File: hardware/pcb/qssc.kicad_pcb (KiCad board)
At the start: 4 copper layers, 130 x 85 mm, 75 parts, among them J1 FT232RL, J10 USB-C, J2 5V Barrel, J3 SMA, J4 Emitter drv, J5 Detector FE, J6 DET_BIAS, J7 RESET, J8 MW_GATE, J9 JTAG, U1 XC7A35T-1CPG236C, U3 ADF4351BCPZ, U5 HMC441LP3E, U7 ADA4530-1, Y1 100MHz TCXO

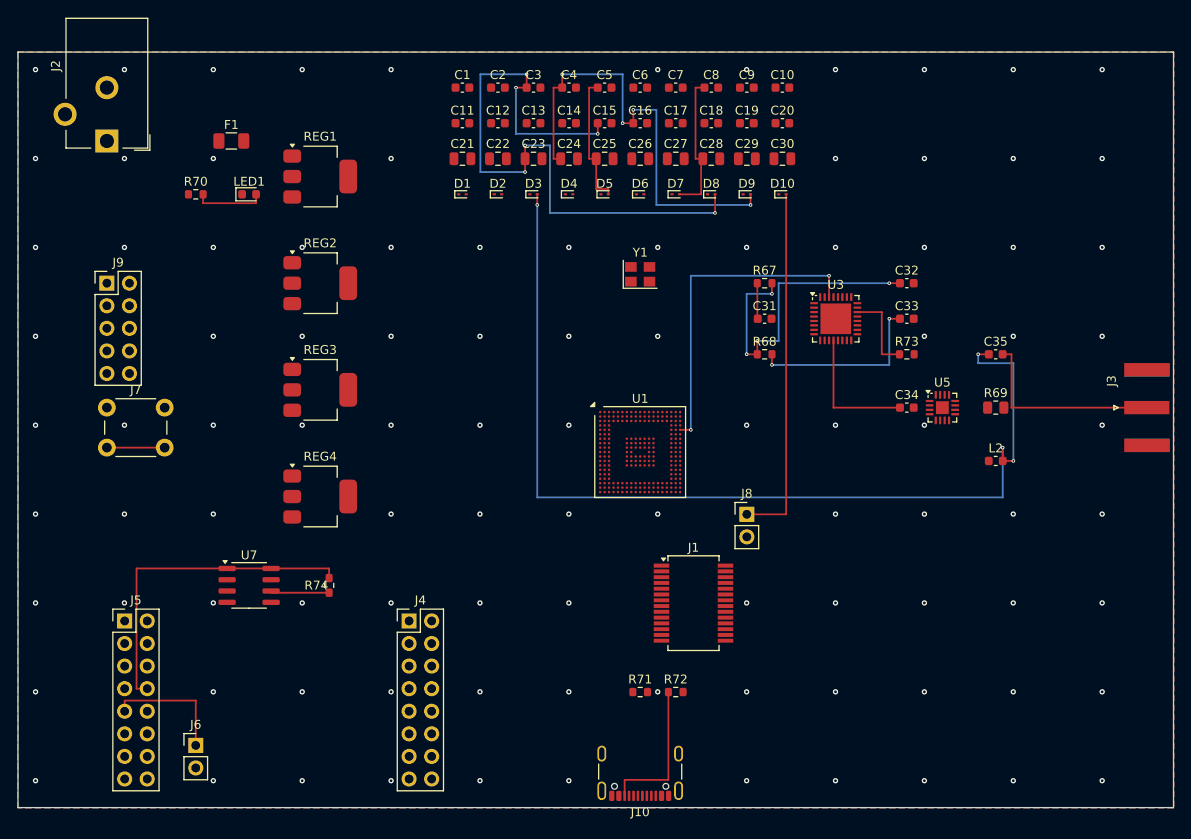
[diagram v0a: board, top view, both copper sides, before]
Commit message: pcb: fix FPGA GND-ball netting (52 balls were wrongly +3V3) + full CPG236 ball map
The FPGA power/ground net map was missing the "GND" key in _FPGA_PWR_NET,
so all 52 GND balls fell through the `else "+3V3"` branch (intended only for
VCCO_* banks) and were netted +3V3 — electrically wrong though DRC appeared
clean (all pads on the same wrong net, no conflict).

Fix: add "GND":"GD" to _FPGA_PWR_NET. Now A1/W1/... -> GND as datasheet
intended.

Verified:
  fpga_net_map(): A1->GND, W1->GND, GND=67 balls, +3V3=30, +1V0=8, +1V8=3
  saved PCB sexp: 157 pads netted (67 GND/30 +3V3/8 +1V0/3 +1V8), 81 NC spare-IO
  kicad-cli pcb drc: 0 violations, 0 unconnected, 0 footprint errors

Co-Authored-By: Claude <noreply@anthropic.com>
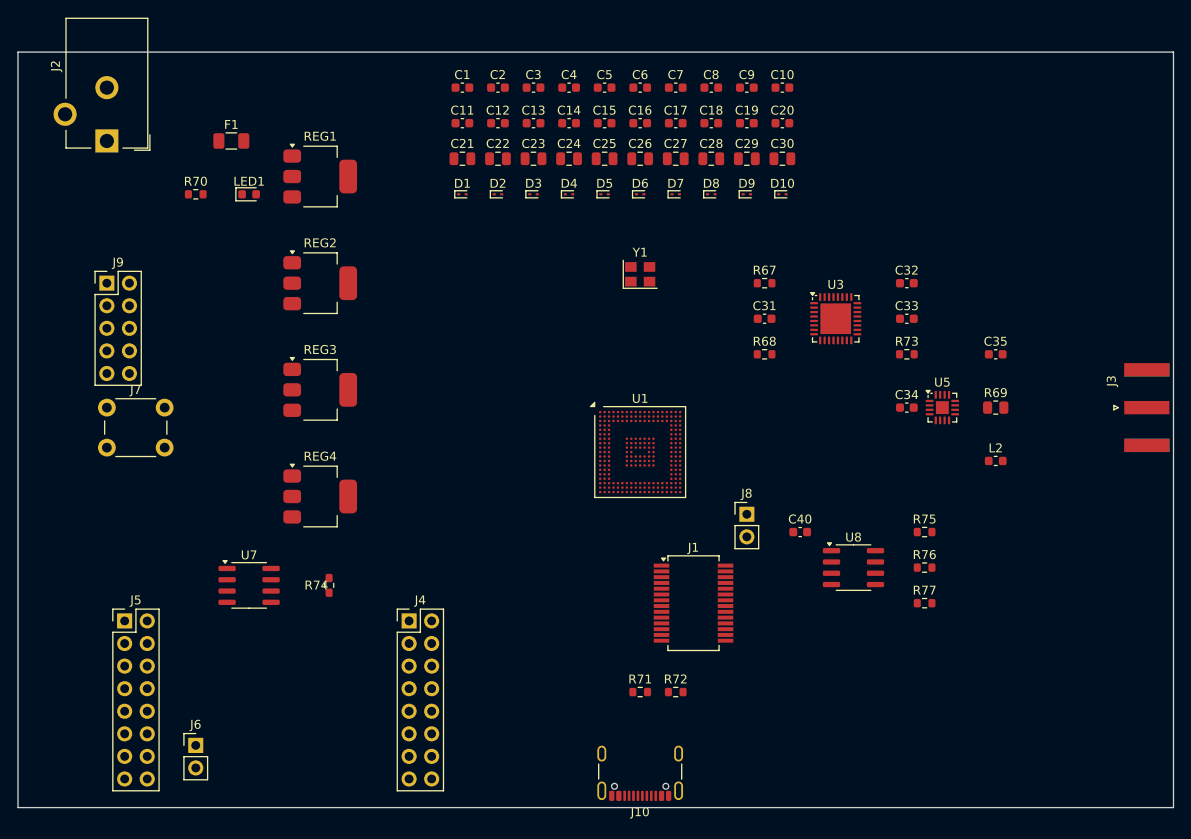
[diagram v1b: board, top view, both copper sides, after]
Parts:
- added C40: 100nF, C_0603_1608Metric, F.Cu at (88.0, 54.0)
- added R75: 4.7k, R_0603_1608Metric, F.Cu at (102.0, 54.0)
- added R76: 4.7k, R_0603_1608Metric, F.Cu at (102.0, 58.0)
- added R77: 4.7k, R_0603_1608Metric, F.Cu at (102.0, 62.0)
- added U8: W25Q128JVSIQ, SOIC-8_3.9x4.9mm_P1.27mm, F.Cu at (94.0, 58.0)
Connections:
- U1 pad A1: (no net) -> GND
- U1 pad A12: (no net) -> TIA_OUT
- U1 pad A13: (no net) -> GND
- U1 pad A14: (no net) -> refclk_out
- U1 pad A15: (no net) -> mod_sync
- U1 pad A16: (no net) -> clk_100mhz
- U1 pad A17: (no net) -> mw_gate
- U1 pad A18: (no net) -> SPI_CLK
- U1 pad A19: (no net) -> GND
- U1 pad A3: (no net) -> GND
- U1 pad A5: (no net) -> GND
- U1 pad A7: (no net) -> GND
- U1 pad A9: (no net) -> GND
- U1 pad B1: (no net) -> GND
- U1 pad B12: (no net) -> VREFP
- U1 pad B13: (no net) -> GND
- U1 pad B14: (no net) -> GND
- U1 pad B15: (no net) -> SPI_DATA
- U1 pad B16: (no net) -> ADF_MUXOUT
- U1 pad B17: (no net) -> emitter_rows0
- U1 pad B18: (no net) -> emitter_rows3
- U1 pad B19: (no net) -> +3V3
- U1 pad B3: (no net) -> GND
- U1 pad B5: (no net) -> GND
- U1 pad B7: (no net) -> GND
- U1 pad B9: (no net) -> GND
- U1 pad C1: (no net) -> GND
- U1 pad C10: (no net) -> GND
- U1 pad C11: (no net) -> SPI_CCLK
- U1 pad C12: (no net) -> GND
- U1 pad C13: (no net) -> +1V8
- U1 pad C14: (no net) -> +3V3
- U1 pad C15: (no net) -> emitter_rows4
- U1 pad C16: (no net) -> emitter_rows6
- U1 pad C17: (no net) -> emitter_cols0
- U1 pad C18: refclk_25m -> +3V3
- U1 pad C19: (no net) -> GND
- U1 pad C2: (no net) -> GND
- U1 pad C3: (no net) -> GND
- U1 pad C4: (no net) -> GND
- U1 pad C5: (no net) -> GND
- U1 pad C6: (no net) -> GND
- U1 pad C7: (no net) -> GND
- U1 pad C8: (no net) -> TCK
- U1 pad C9: (no net) -> +3V3
- U1 pad D18: SPI_CLK -> SPI_D0
- U1 pad D19: SPI_DATA -> SPI_D1
- U1 pad D3: (no net) -> GND
- U1 pad E1: (no net) -> GND
- U1 pad E17: (no net) -> GND
- U1 pad E19: ADF_MUXOUT -> (no net)
- U1 pad E2: (no net) -> GND
- U1 pad E3: (no net) -> GND
- U1 pad F1: (no net) -> GND
- U1 pad F17: (no net) -> +3V3
- U1 pad F18: det_mux_sel5 -> SPI_D3
- U1 pad F19: (no net) -> GND
- U1 pad F2: (no net) -> GND
- U1 pad F3: (no net) -> GND
- U1 pad G1: (no net) -> GND
- U1 pad G10: (no net) -> +1V0
- U1 pad G11: (no net) -> GND
- U1 pad G12: (no net) -> +3V3
- U1 pad G13: (no net) -> +3V3
- U1 pad G18: det_mux_sel3 -> SPI_D2
- U1 pad G19: (no net) -> emitter_cols2
- U1 pad G7: (no net) -> GND
- U1 pad G8: (no net) -> GND
- U1 pad G9: (no net) -> GND
- U1 pad H10: (no net) -> +1V0
- U1 pad H11: (no net) -> GND
- U1 pad H12: (no net) -> GND
- U1 pad H13: (no net) -> +1V8
- U1 pad H18: (no net) -> GND
- U1 pad H19: (no net) -> emitter_cols3
- U1 pad H3: (no net) -> +3V3
- U1 pad H7: (no net) -> GND
- U1 pad H8: (no net) -> GND
- U1 pad H9: (no net) -> GND
- U1 pad J10: (no net) -> +1V0
- U1 pad J11: (no net) -> GND
- U1 pad J12: (no net) -> GND
- U1 pad J13: (no net) -> +1V8
- U1 pad J18: (no net) -> emitter_cols5
- U1 pad J19: (no net) -> det_mux_sel1
- U1 pad J7: (no net) -> +3V3
- U1 pad J8: (no net) -> GND
- U1 pad J9: (no net) -> GND
- U1 pad K1: (no net) -> +3V3
- U1 pad K12: (no net) -> +3V3
- U1 pad K13: (no net) -> +3V3
- U1 pad K19: (no net) -> SPI_CS
- U1 pad K7: (no net) -> +3V3
- U1 pad K8: (no net) -> GND
- U1 pad L10: (no net) -> +1V0
- U1 pad L11: (no net) -> GND
- U1 pad L12: (no net) -> +3V3
- U1 pad L13: (no net) -> +3V3
- U1 pad L17: (no net) -> det_mux_sel3
- U1 pad L19: (no net) -> GND
- U1 pad L7: (no net) -> +3V3
- U1 pad L8: (no net) -> GND
- U1 pad L9: (no net) -> GND
- U1 pad M10: (no net) -> +1V0
- U1 pad M11: (no net) -> +1V0
- U1 pad M12: (no net) -> +3V3
- U1 pad M13: (no net) -> GND
- U1 pad M17: emitter_rows4 -> +3V3
- U1 pad M19: (no net) -> det_mux_sel5
- U1 pad M7: (no net) -> +3V3
- U1 pad M8: (no net) -> +3V3
- U1 pad M9: (no net) -> GND
- U1 pad N10: (no net) -> +1V0
- U1 pad N11: (no net) -> +1V0
- U1 pad N12: (no net) -> GND
- U1 pad N13: (no net) -> GND
- U1 pad N7: (no net) -> +3V3
- U1 pad N8: (no net) -> +3V3
- U1 pad N9: (no net) -> GND
- U1 pad P17: UART_RX -> rx
- U1 pad P18: UART_TX -> tx
- U1 pad P2: (no net) -> GND
- U1 pad R1: (no net) -> +3V3
- U1 pad R17: emitter_cols3 -> +3V3
- U1 pad T19: (no net) -> GND
- U1 pad U10: (no net) -> GND
- U1 pad U11: (no net) -> CONF_INIT
- U1 pad U12: (no net) -> CONF_DONE
- U1 pad U13: (no net) -> +3V3
- U1 pad U6: (no net) -> GND
- U1 pad U9: (no net) -> GND
- U1 pad V1: (no net) -> +3V3
- U1 pad V10: (no net) -> CONF_PROG
- U1 pad V11: (no net) -> +3V3
- U1 pad V12: (no net) -> +3V3
- U1 pad V18: (no net) -> GND
- U1 pad V6: (no net) -> +3V3
- U1 pad V9: (no net) -> +3V3
- U1 pad W1: (no net) -> GND
- U1 pad W10: (no net) -> TDI
- U1 pad W11: (no net) -> GND
- U1 pad W12: (no net) -> GND
- U1 pad W8: (no net) -> TDO
- U1 pad W9: (no net) -> TMS
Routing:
- net RF_AMP_OUT: track 111.9 -> 0.00 mm, vias 4 -> 0
- net +1V0: track 73.6 -> 0.00 mm, vias 6 -> 0
- net +5V_RF: track 51.4 -> 0.00 mm, vias 4 -> 0
- net mw_gate: track 40.4 -> 0.00 mm
- net DET_IN: track 37.5 -> 0.00 mm
- net ADF_MUXOUT: track 36.5 -> 0.00 mm, vias 2 -> 0
- net LF_MID: track 36.1 -> 0.00 mm, vias 4 -> 0
- net J3_SIG: track 22.2 -> 0.00 mm
- net LF_OUT: track 20.8 -> 0.00 mm, vias 2 -> 0
- net CC2: track 16.6 -> 0.00 mm
- net +1V8: track 16.5 -> 0.00 mm
- net +5V: track 15.1 -> 0.00 mm
- net RF_OUT: track 15.0 -> 0.00 mm
- net DET_BIAS: track 14.2 -> 0.00 mm
- net RSET: track 9.49 -> 0.00 mm
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- removed copper zone on In2.Cu, net +3V3
- removed copper zone on B.Cu, net GND
- removed copper zone on F.Cu, net GND
- removed copper zone on In1.Cu, net GND

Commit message: fpga: ground all 22 MGT_GND balls + reproducible CPG236 ball-map generator
The hand-built ball map grounded only 10 of the 22 MGT_GND balls (A2,A4,
A6,A8,A10,B2,B4,B6,B8,B10,D1,D2 were left floating). DRC was clean because
unnetted BGA pads aren't flagged -- but per UG475 every MGT_GND pad on the
CPG236 package must tie to ground even though XC7A35T has no MGT transceiver.

Add tools/gen_fpga_ballmap.py: parses the real FPGA_Xilinx_Artix7:
XC7A35T-CPG236 symbol (238 pads) and emits .tmpwork/fpga_cpg236_map.json,
deriving the power dict authoritatively from pin names so a ground/supply
ball can never be silently dropped. signals/config/jtag/xadc sections are
design choices preserved (all verified on real IO / dedicated pins; clk
on A16 = IO_L12P_T1_MRCC_16, a clock-capable pin).

Verified after regen:
  238 pads total, 168 netted, 70 NC (68 spare IO + DXP/DXN temp diode)
  GND=79 (52 GND + 22 MGT_GND + GNDADC + VREFN + VN + M1 + M2)
  A2/A10 -> GND (were floating); A12 -> TIA_OUT; A16 -> clk_100mhz
  kicad-cli pcb drc: 0 violations, 0 unconnected

Co-Authored-By: Claude <noreply@anthropic.com>
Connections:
- U1 pad A10: (no net) -> GND
- U1 pad A2: (no net) -> GND
- U1 pad A4: (no net) -> GND
- U1 pad A6: (no net) -> GND
- U1 pad A8: (no net) -> GND
- U1 pad B10: (no net) -> GND
- U1 pad B2: (no net) -> GND
- U1 pad B4: (no net) -> GND
- U1 pad B6: (no net) -> GND
- U1 pad B8: (no net) -> GND
- U1 pad D1: (no net) -> GND
- U1 pad D2: (no net) -> GND
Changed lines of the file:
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@@
 			(property pad_prop_bga)
 			(layers "F.Cu" "F.Paste" "F.Mask")
+			(net 16 "GND")
 		)
 		(pad "A3" smd circle
@@
 			(property pad_prop_bga)
 			(layers "F.Cu" "F.Paste" "F.Mask")
+			(net 16 "GND")
 		)
 		(pad "A5" smd circle
@@
 			(property pad_prop_bga)
 			(layers "F.Cu" "F.Paste" "F.Mask")
+			(net 16 "GND")
 		)
 		(pad "A7" smd circle
@@
 			(property pad_prop_bga)
 			(layers "F.Cu" "F.Paste" "F.Mask")
+			(net 16 "GND")
 		)
 		(pad "A9" smd circle
@@
 			(property pad_prop_bga)
 			(layers "F.Cu" "F.Paste" "F.Mask")
+			(net 16 "GND")
 		)
 		(pad "A11" smd circle
@@
 			(property pad_prop_bga)
 			(layers "F.Cu" "F.Paste" "F.Mask")
+			(net 16 "GND")
 		)
 		(pad "B3" smd circle
@@
 			(property pad_prop_bga)
 			(layers "F.Cu" "F.Paste" "F.Mask")
+			(net 16 "GND")
 		)
 		(pad "B5" smd circle
@@
 			(property pad_prop_bga)
 			(layers "F.Cu" "F.Paste" "F.Mask")
+			(net 16 "GND")
 		)
 		(pad "B7" smd circle
@@
 			(property pad_prop_bga)
 			(layers "F.Cu" "F.Paste" "F.Mask")
+			(net 16 "GND")
 		)
 		(pad "B9" smd circle
@@
 			(property pad_prop_bga)
 			(layers "F.Cu" "F.Paste" "F.Mask")
+			(net 16 "GND")
 		)
 		(pad "B11" smd circle
@@
 			(property pad_prop_bga)
 			(layers "F.Cu" "F.Paste" "F.Mask")
+			(net 16 "GND")
 		)
 		(pad "D2" smd circle
@@
 			(property pad_prop_bga)
 			(layers "F.Cu" "F.Paste" "F.Mask")
+			(net 16 "GND")
 		)
 		(pad "D3" smd circle

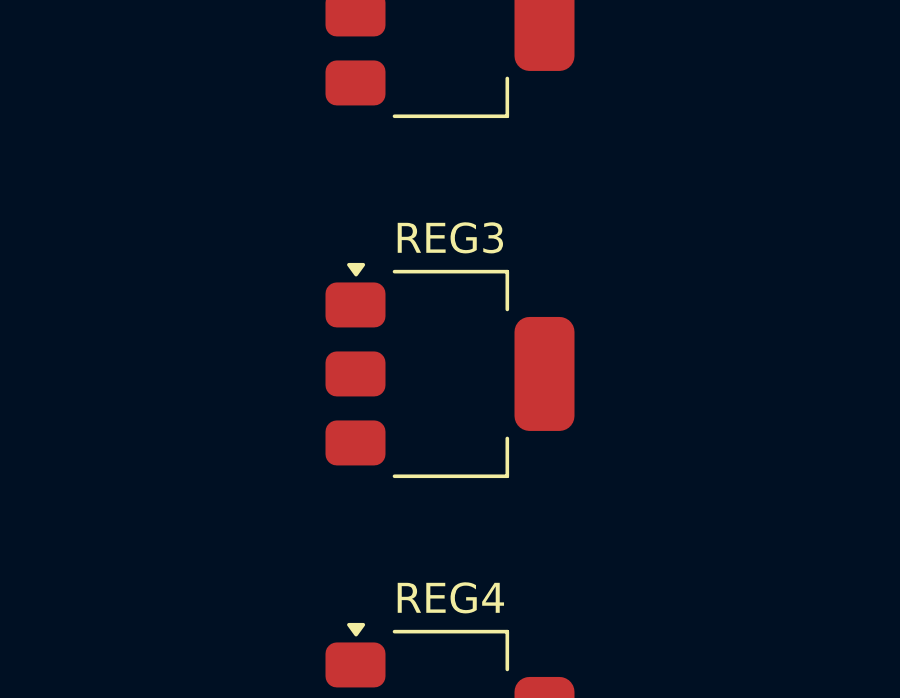
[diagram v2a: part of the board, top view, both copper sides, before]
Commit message: pcb: replace fake AMS1117-1.0 with real AP2127K-1.0 + VREFP PWR_FLAG
AMS1117 has no 1.0 V option (min fixed output 1.5 V), so the VCCINT=1.0 V
rail's "AMS1117-1.0" was a non-existent part. Use the AP2127K-1.0 (Diodes
Inc, 600 mA, SOT-23-5) with its datasheet pinout (1=VIN 2=GND 3=EN 4=BP
5=VOUT): VIN/EN tied to +5V, BP decoupled via C41 10nF, VOUT->+1V0 with
10uF/100nF local decoupling (C43/C44) and a 10uF input cap (C42).

Also fix a pre-existing ERC error: U1 pin B12 (VREFP, power input) was
not driven -- the Artix-7 XADC internal 1.25 V reference drives VREFP but
ERC cannot see it. Add #FLG4 PWR_FLAG on VREFP.

Verified:
  kicad-cli sch erc: 0 errors / 145 warnings (all endpoint_off_grid, benign)
  kicad-cli pcb drc: 0 violations / 0 unconnected / 0 footprint errors
  REG3 pads netted: 1->+5V 2->GND 3->+5V 4->BP_1V0 5->+1V0 (datasheet pinout)
  +1V0 rail: 17 pins (REG3 VOUT + 8x FPGA VCCINT + bulk/decoupling/ESD)
  ruff clean; 88 components (was 75)

Co-Authored-By: Claude <noreply@anthropic.com>
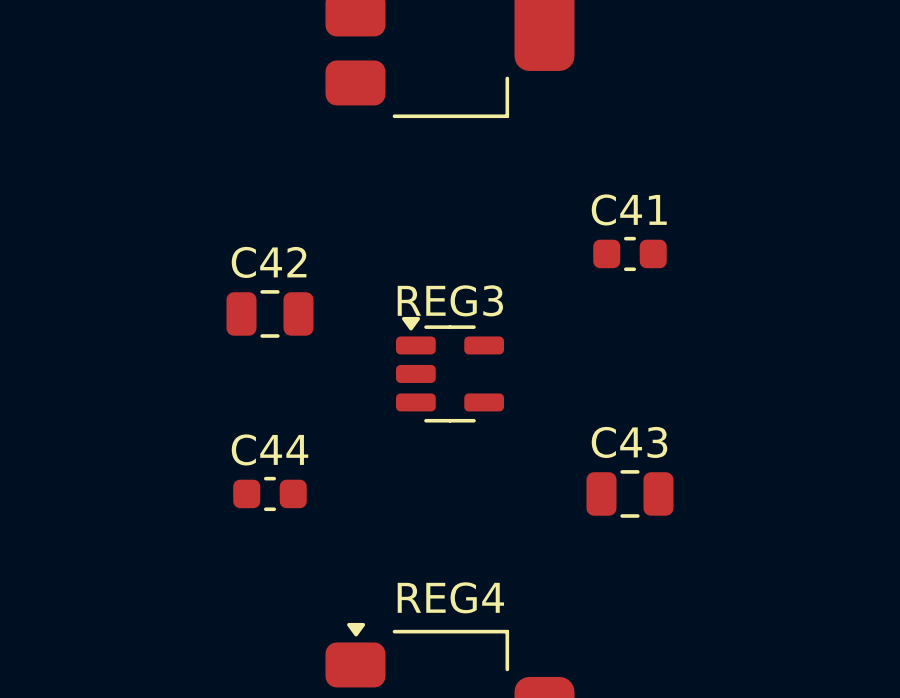
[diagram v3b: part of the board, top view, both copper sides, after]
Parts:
- added C41: 10nF, C_0603_1608Metric, F.Cu at (40.0, 34.0)
- added C42: 10uF, C_0805_2012Metric, F.Cu at (28.0, 36.0)
- added C43: 10uF, C_0805_2012Metric, F.Cu at (40.0, 42.0)
- added C44: 100nF, C_0603_1608Metric, F.Cu at (28.0, 42.0)
- REG3: value AMS1117-1.0 -> AP2127K-1.0; footprint SOT-223-3_TabPin2 -> SOT-23-5
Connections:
- REG3 pad 1: GND -> +5V
- REG3 pad 2: +1V0 -> GND

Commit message: PCB: conectador board-to-board J11 (Samtec LSHM-130) + corrije cortocircuito esquemático del FPGA
* Añade J11 (Samtec LSHM-130 2x30 0.5 mm) como "socket" del módulo hija con
  front-end analógico (MUX 64:1 + TIA + driver CQD + Peltier). 60 pines netted:
  filas/cols del emisor (8+8), det_mux_sel[5:0], mod_sync, TIA_OUT, TIA_REF,
  DET_BIAS, THRM, +3V3/+5V/+7V_EMIT, y GND en todos los pines pares (retorno
  por señal). Sustituye el bloque analógico J4/J5/J6/R74/U7 placeholder.
* REG3 pasa a AP2127K-1.0 (Diodes Inc SOT-23-5): LDO real de 1.0 V para
  VCCINT — AMS1117 no tiene opción 1.0 V (mín 1.5 V). Símbolo autorizado por
  datasheet (1=VIN 2=GND 3=EN 4=BP 5=VOUT) + descargas C41-C44 + PWR_FLAG VREFP.
* Corrige cortocircuito esquemático en fpga_pin_list: las columnas de pines
  señal (x=±17.78) coincidían en la esquina con la fila GND inferior (y=10.16),
  dejando dos etiquetas (señal + GND) en el mismo punto → ERC multiple_net_names
  fundía la señal a GND (le pasó a emitter_cols0/C17). Movido a x=±50.8 (fuera
  del alcance de la fila, máx 49.53), on-grid, sin colisión.
* Movido J11 a (24,64): en (30,45) solapaba courtyards de C43/C44/REG4 y
  cortocircuitaba pads de descarga con pads de emitter_cols (DRC shorting_items).

Verificación: ERC 0 errores; DRC 0 errores/0 warnings/0 desconectados;
pytest 122 passed 2 skipped; XDC ports ok; emitter_cols0 = net 56 ≠ GND net 17.

Co-Authored-By: Claude <noreply@anthropic.com>
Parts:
- removed J4: Emitter drv, PinHeader_2x08_P2.54mm_Vertical
- removed J5: Detector FE, PinHeader_2x08_P2.54mm_Vertical
- removed J6: DET_BIAS, PinHeader_1x02_P2.54mm_Vertical
- removed R74: 1M, R_0603_1608Metric
- removed U7: ADA4530-1, SOIC-8_3.9x4.9mm_P1.27mm
- added J11: Samtec LSHM-130, Samtec_LSHM-130-xx.x-x-DV-N_2x30_P0.50mm_Vertical, F.Cu at (24.0, 64.0)

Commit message: chip module: place discrete MOSFET emitter crossbar (+5V), eliminate +7V_EMIT
Emitter driver for the 8x8 CQD matrix is now placed on the swappable chip
module as the simplest-functional topology (29 parts, no boost / no DAC /
no TLC5955): 2x 74HCT240 inverting level-shifters (3.3V FPGA -> 0/5V gate
drive, HCT TTL thresholds) + 8x AO3401A P-MOS high-side row switches +
8x AO3400A N-MOS low-side column sinks + 8x 220R set resistors + 3
decoupling. One pixel at a time, ~9mA at 2.2V headroom, matching
emitter_array.v (rows active-HIGH / cols active-LOW one-hot, idle all OFF).

Chip ER/EC pads rewired through the driver (ER{i}->emitter_anode{i},
EC{i}->emitter_cathode{i}); J1 still carries emitter_rows/cols -> 74HCT240
inputs. +7V_EMIT rail fully deleted on both boards: J1/J11 pin 59 -> GND
(extra pulsed-current return; connectors stay pin-for-pin mated), module
POWER_PINS/POWER_NETS/C6/#FLG3 removed. TIA is photovoltaic / zero-bias
(no MCP4921 DAC; DET_BIAS is a reserved spare). Module widened 70->85x50mm.

Verified headless: module ERC 0 errors / 53 warnings; module DRC 0
violations; main board ERC 0 errors / 139 warnings, DRC 0 violations.
pytest 122 passed / 2 skipped; ruff CI-gate clean. HARDWARE_DESIGN.md
\S1B/\S2/\S3/\S7/\S8/\S11/\S12/\S13/\S15A updated. RTL/XDC/sim/synth
untouched; new ~24 nets not yet routed (deferred GUI batch).

Co-Authored-By: Claude <noreply@anthropic.com>
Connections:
- J11 pad 59: +7V_EMIT -> GND
